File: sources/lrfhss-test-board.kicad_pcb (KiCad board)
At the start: 2 copper layers, 80.6 x 79 mm, 19 parts, among them J1 SSW-103-01-L-S, J10 SSW-103-01-L-S, J11 SSW-103-01-L-S, J12 SSW-103-01-L-S, J13 09665526616, J2 SSW-103-01-L-S, J3 SSW-103-01-L-S, J4 SSW-103-01-L-S, J5 SSW-103-01-L-S, J6 SSW-103-01-L-S, J7 SSW-103-01-L-S, J8 SSW-103-01-L-S, J9 SSW-103-01-L-S

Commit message: feat: add initial version of the schematic
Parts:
- removed the G*** at (97.3, 54.0)
- removed J10, J11, J12, J5, J6, J7, J8, J9: SSW-103-01-L-S, footprints:SSW-103-01-L-S
- removed J13: 09665526616, footprints:966552616
- added C1: 1uF, footprints:CAP0805, F.Cu at (62.7, 111.3)
- added C2: 1uF, footprints:CAP0805, F.Cu at (55.7, 115.1)
- added C3: 47uF, footprints:CAP2917POL, F.Cu at (97.4, 65.0)
- added C4: 100nF, footprints:CAP0603, F.Cu at (102.1, 62.6)
- added R1: 1M, footprints:RES0402, F.Cu at (47.2, 107.6)
- added R2: 5.11k, footprints:RES0402, F.Cu at (50.4, 103.3)
- added R3: 5.11k, footprints:RES0402, F.Cu at (50.4, 100.3)
- added R4: 1k, footprints:RES0603, F.Cu at (54.5, 99.1)
- added U1: LoRa126XF30, footprints:LoRa126XF30, F.Cu at (81.3, 75.9)
- added U2: AMS1117-3.3, Package_TO_SOT_SMD:SOT-223-3_TabPin2, F.Cu at (56.6, 109.1)
- J1: value SSW-103-01-L-S -> USB-C; footprint footprints:SSW-103-01-L-S -> Connector_USB:USB_C_Receptacle_HRO_TYPE-C-31-M-12
- J2, J3: value SSW-103-01-L-S -> Molex_PicoBlade_53398-0271_1x02-1MP_P1.25mm_Vertical; footprint footprints:SSW-103-01-L-S -> footprints:532610271
- J4: value SSW-103-01-L-S -> Molex_PicoBlade_53398-0471_1x04-1MP_P1.25mm_Vertical; footprint footprints:SSW-103-01-L-S -> footprints:532610471
- moved G*** 69.7 mm to (62.5, 43.1)
- moved J4 58.0 mm to (43.0, 67.6)
- moved J3 44.6 mm to (43.0, 90.5)
- moved J2 30.1 mm to (43.0, 79.7)
- moved J1 25.6 mm to (43.6, 101.5)
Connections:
- J2 pad 1: /V_{G2} -> /CTRL0
- J2 pad 2: /V_{D2} -> /CTRL1
- J2 pad 3: /V_{S2} -> unconnected-(J2-MNTF-Pad3)
- J3 pad 1: /V_{G3} -> /DATA0
- J3 pad 2: /V_{D3} -> /DATA1
- J3 pad 3: /V_{S3} -> unconnected-(J3-MNTF-Pad3)
- J4 pad 1: /V_{G4} -> /SPI0
- J4 pad 2: /V_{D4} -> /SPI1
- J4 pad 3: /V_{S4} -> /SPI2
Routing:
- net /V_{G9}: track 89.5 -> 0.00 mm, vias 1 -> 0
- net /V_{G12}: track 89.5 -> 0.00 mm, vias 1 -> 0
- net /V_{D9}: track 82.2 -> 0.00 mm
- net /V_{D12}: track 82.2 -> 0.00 mm
- net /V_{S12}: track 76.3 -> 0.00 mm
- net /V_{S9}: track 76.3 -> 0.00 mm
- net /V_{G10}: track 69.5 -> 0.00 mm
- net /V_{G11}: track 69.5 -> 0.00 mm
- net /V_{D10}: track 68.6 -> 0.00 mm
- net /V_{D11}: track 68.6 -> 0.00 mm
- net /V_{S10}: track 66.3 -> 0.00 mm
- net /V_{S11}: track 66.3 -> 0.00 mm
- net /V_{D5}: track 54.6 -> 0.00 mm
- net /V_{D8}: track 54.6 -> 0.00 mm
- net /V_{G5}: track 53.8 -> 0.00 mm
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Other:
- board text removed: "V_{D10}"
- board text removed: "V_{D11}"
- board text removed: "V_{D12}"
- board text removed: "V_{D1}"
- board text removed: "V_{D2}"
- board text removed: "V_{D3}"
- board text removed: "V_{D4}"
- board text removed: "V_{D5}"
- board text removed: "V_{D6}"
- board text removed: "V_{D7}"
- board text removed: "V_{D8}"
- board text removed: "V_{D9}"
- board text removed: "V_{G10}"
- board text removed: "V_{G11}"
- board text removed: "V_{G12}"
- board text removed: "V_{G1}"
- board text removed: "V_{G2}"
- board text removed: "V_{G3}"
- board text removed: "V_{G4}"
- board text removed: "V_{G5}"
- board text removed: "V_{G6}"
- board text removed: "V_{G7}"
- board text removed: "V_{G8}"
- board text removed: "V_{G9}"
- board text removed: "V_{S10}"
- board text removed: "V_{S11}"
- board text removed: "V_{S12}"
- board text removed: "V_{S1}"
- board text removed: "V_{S2}"
- board text removed: "V_{S3}"
- board text removed: "V_{S4}"
- board text removed: "V_{S5}"
- board text removed: "V_{S6}"
- board text removed: "V_{S7}"
- board text removed: "V_{S8}"
- board text removed: "V_{S9}"

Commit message: feat: improve schematic and layout
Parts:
- added D1: LED, LED_SMD:LED_0603_1608Metric, F.Cu at (45.8, 107.9)
- added J5: CINCH_142-0701-801, footprints:142-0701-801, F.Cu at (86.5, 90.2)
- J1: footprint Connector_USB:USB_C_Receptacle_HRO_TYPE-C-31-M-12 -> footprints:GENERIC-USB-C
- J2, J3: value Molex_PicoBlade_53398-0271_1x02-1MP_P1.25mm_Vertical -> 532610271
- J4: value Molex_PicoBlade_53398-0471_1x04-1MP_P1.25mm_Vertical -> 532610471
- moved C4 63.9 mm to (45.6, 92.5), turned to -90 degrees
- moved C3 53.4 mm to (50.3, 90.2), turned to 90 degrees
- moved J3 48.9 mm to (86.8, 68.7), turned to 90 degrees
- moved J4 45.2 mm to (86.8, 56.4), turned to 90 degrees
- moved H2 29.9 mm to (87.4, 47.0)
- moved H4 29.4 mm to (87.4, 114.0)
- moved C2 22.9 mm to (74.4, 101.9), turned to -90 degrees
- moved U2 17.8 mm to (74.4, 108.4), turned to -90 degrees
- moved U1 16.4 mm to (65.2, 79.3), turned to 90 degrees
- moved J1 16.2 mm to (55.5, 112.4), turned to 0 degrees
- moved R1 14.9 mm to (61.9, 109.8), turned to 90 degrees
- moved C1 13.3 mm to (72.1, 101.9)
- moved R4 11.1 mm to (47.7, 107.9), turned to 90 degrees
- moved R2 7.25 mm to (57.3, 105.5), turned to -90 degrees
- moved G*** 7.22 mm to (58.1, 48.8)
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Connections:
- J2 pad 1: /CTRL0 -> /CTRL1
- J2 pad 2: /CTRL1 -> /CTRL0
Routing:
- net VBUS: track 0.00 -> 65.6 mm, vias 0 -> 2
- net /SPI3: track 0.00 -> 35.9 mm
- net /DATA0: track 0.00 -> 23.5 mm
- net /SPI0: track 0.00 -> 23.3 mm
- net /SPI1: track 0.00 -> 20.9 mm
- net /DATA1: track 0.00 -> 19.6 mm
- net Net-(J1-SHIELD): track 0.00 -> 19.1 mm
- net /SPI2: track 0.00 -> 18.4 mm
- net ANT: track 0.00 -> 13.1 mm
- net /CTRL1: track 0.00 -> 12.1 mm
- net /CTRL0: track 0.00 -> 12.0 mm
- net GND: track 0.00 -> 4.37 mm, vias 0 -> 19
- net 3V3: track 0.00 -> 2.44 mm
- net Net-(J1-CC2): track 0.00 -> 2.41 mm
- net Net-(J1-CC1): track 0.00 -> 2.40 mm
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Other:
- board size 80.6 x 79 mm -> 51.2 x 73.2 mm

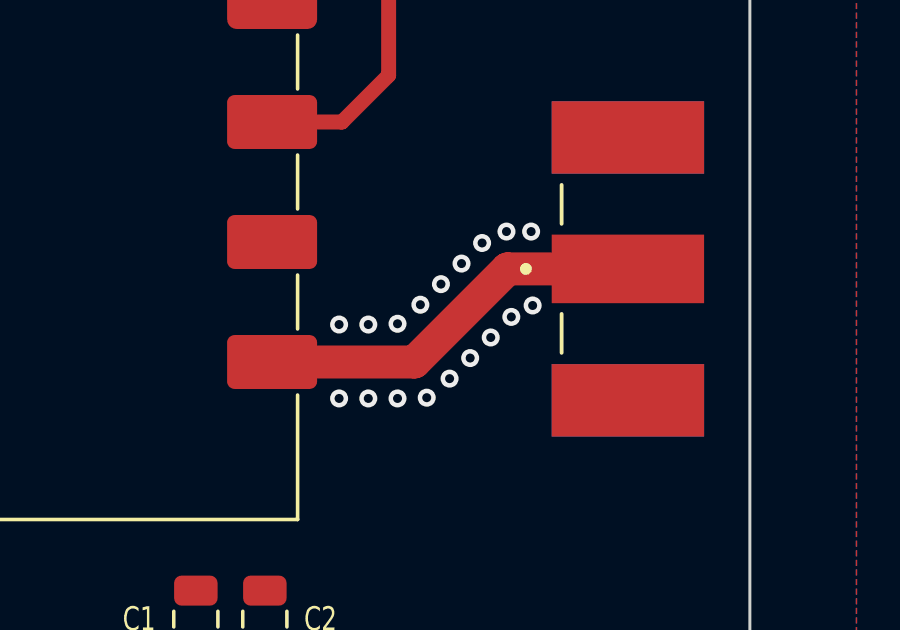
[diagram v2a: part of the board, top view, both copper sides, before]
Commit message: fix: add 3D model to LoRa module
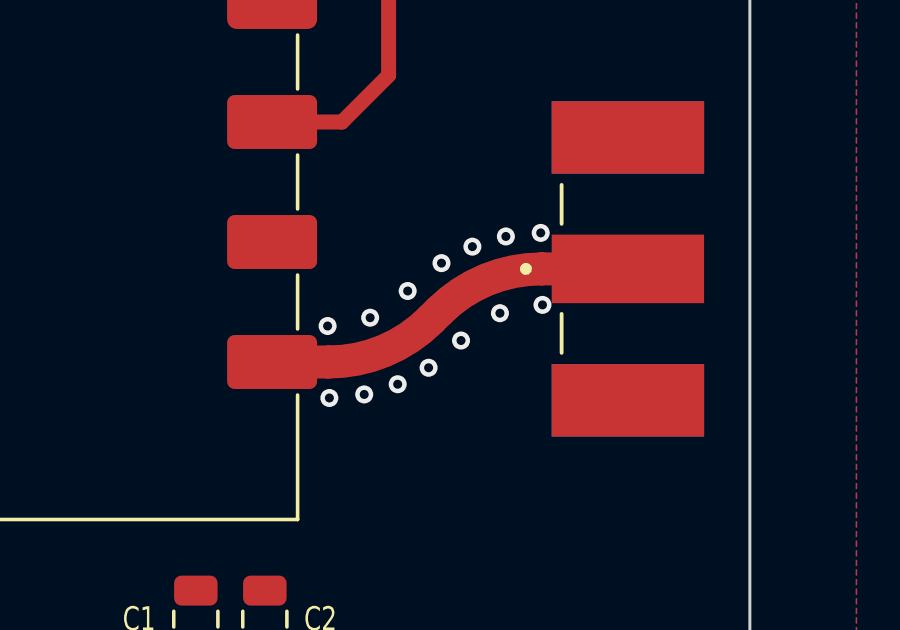
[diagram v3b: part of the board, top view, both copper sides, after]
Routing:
- net GND: vias 19 -> 15

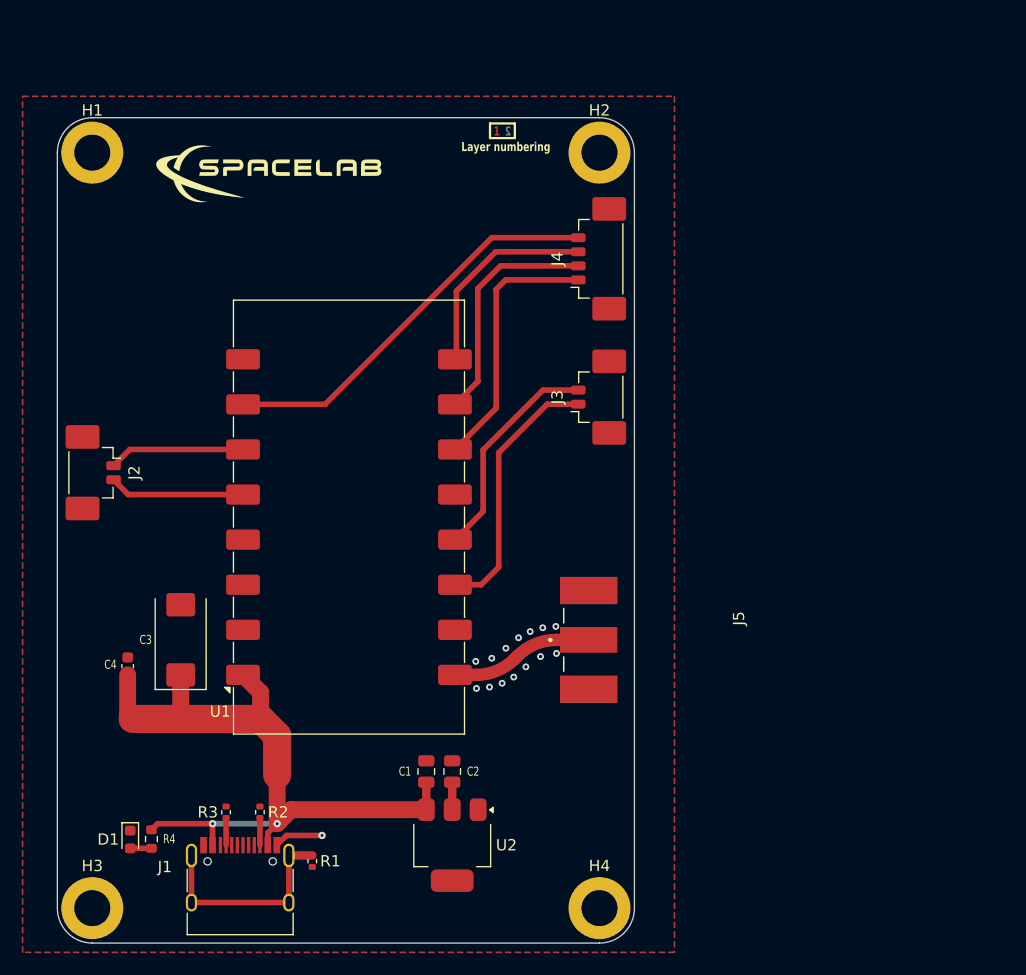
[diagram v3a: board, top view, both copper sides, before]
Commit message: fix: add pins to interface with jumpers and some connectors for power
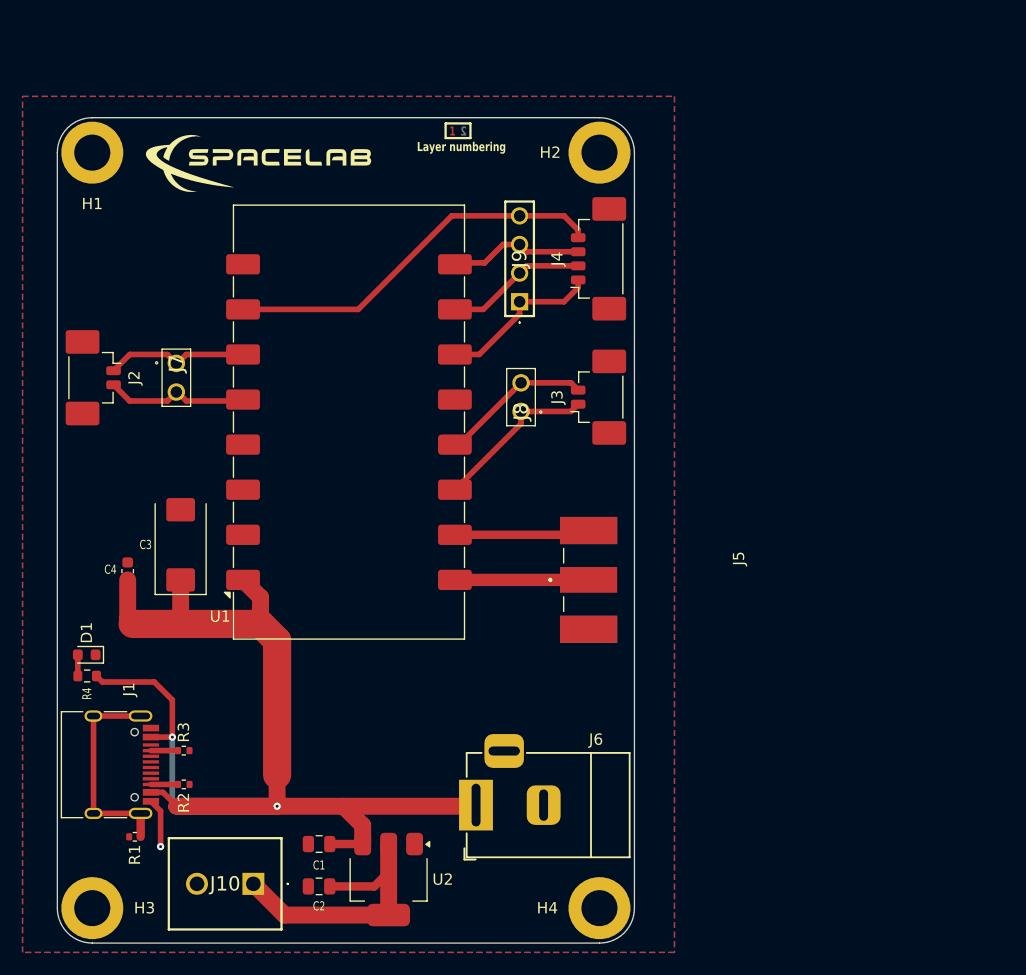
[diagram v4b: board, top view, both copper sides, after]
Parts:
- added J10: Screw_Terminal_01x02, footprints:MV-152, F.Cu at (56.7, 111.8)
- added J6: Barrel_Jack_Switch_Pin3Ring, footprints:DC_Power_Jack_PCB_Mounted_2.1mm, F.Cu at (76.5, 104.9)
- added J7: Conn_01x02_Pin, footprints:TSW-102-07-G-S, F.Cu at (49.9, 65.7)
- added J8: Conn_01x02_Pin, footprints:TSW-102-07-G-S, F.Cu at (80.5, 69.9)
- added J9: Conn_01x04_Pin, footprints:TSW-104-07-G-S, F.Cu at (80.3, 60.2)
- J5: value CINCH_142-0701-801 -> 142-0701-801
- moved D1 16.8 mm to (41.9, 91.5), turned to 180 degrees
- moved J1 16.4 mm to (43.6, 101.3), turned to -90 degrees
- moved R1 15.9 mm to (46.2, 107.7), turned to 0 degrees
- moved C2 15.6 mm to (62.5, 112.1), turned to 0 degrees
- moved R4 15.5 mm to (42.0, 93.4), turned to 0 degrees
- moved C1 11.5 mm to (62.5, 108.3), turned to 0 degrees
- moved C3 8.43 mm to (50.3, 81.8)
- moved C4 8.43 mm to (45.6, 84.1)
- moved J2 8.43 mm to (43.1, 66.9)
- moved U1 8.43 mm to (65.2, 70.9)
- moved R2 7.19 mm to (50.5, 103.0), turned to 180 degrees
- moved R3 6.63 mm to (50.5, 100.0), turned to 180 degrees
- moved U2 6.41 mm to (68.7, 111.5)
- moved J5 5.32 mm to (86.5, 84.9)
- moved G*** 1.30 mm to (57.2, 47.9)
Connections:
- J5 pad S1: GND -> GND1
- J5 pad S2: GND -> GND1
- J5 pad S3: GND -> GND1
- J5 pad S4: GND -> GND1
- U1 pad 15: GND -> GND1
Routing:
- net VBUS: track 65.6 -> 105.5 mm
- net 3V3: track 2.44 -> 27.7 mm
- net GND1: track 0.00 -> 11.5 mm
- net /SPI0: track 23.3 -> 14.9 mm
- net /DATA0: track 23.5 -> 15.1 mm
- net /SPI1: track 20.9 -> 12.5 mm
- net /SPI2: track 18.4 -> 11.8 mm
- net /DATA1: track 19.6 -> 13.5 mm
- net /SPI3: track 35.9 -> 34.4 mm
- net ANT: track 12.7 -> 11.9 mm
- net /CTRL1: track 12.1 -> 12.7 mm
- net /CTRL0: track 12.0 -> 12.6 mm
- net GND: vias 15 -> 1

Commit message: fix: add final version to fabricate the board at INEP
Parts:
- removed J6: Barrel_Jack_Switch_Pin3Ring, footprints:DC_Power_Jack_PCB_Mounted_2.1mm
- added J11: Screw_Terminal_01x02, footprints:MV-152, F.Cu at (102.4, 100.1)
- C3: footprint footprints:CAP2917POL -> footprints:CAP47UELECTROLYTIC
- moved C3 17.4 mm to (67.4, 84.9)
- moved H2 17.1 mm to (104.6, 47.0)
- moved H4 17.1 mm to (104.6, 114.0)
- moved U2 17.1 mm to (85.9, 111.5)
- moved C4 17.1 mm to (62.7, 84.1)
- moved D1 17.1 mm to (59.1, 91.5)
- moved G*** 17.1 mm to (74.3, 47.9)
- moved J1 17.1 mm to (60.7, 101.3)
- moved J10 17.1 mm to (73.9, 111.8)
- moved J2 17.1 mm to (60.2, 66.9)
- moved J7 17.1 mm to (67.0, 65.7)
- moved R2 17.1 mm to (67.7, 103.0)
- moved C1 17.1 mm to (79.7, 108.3)
- moved C2 17.1 mm to (79.7, 112.1)
- moved H1 17.1 mm to (59.6, 47.0)
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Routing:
- net VBUS: track 105.5 -> 115.9 mm
- net GND: track 4.37 -> 0.00 mm, vias 1 -> 15
